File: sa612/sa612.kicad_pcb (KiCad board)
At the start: 2 copper layers, 12 parts, among them J1 RF_IN, J2 PWR, J3 OSC_IN, J4 IF_OUT, U1 SA612, U2 MCP1700-5002E_SOT23

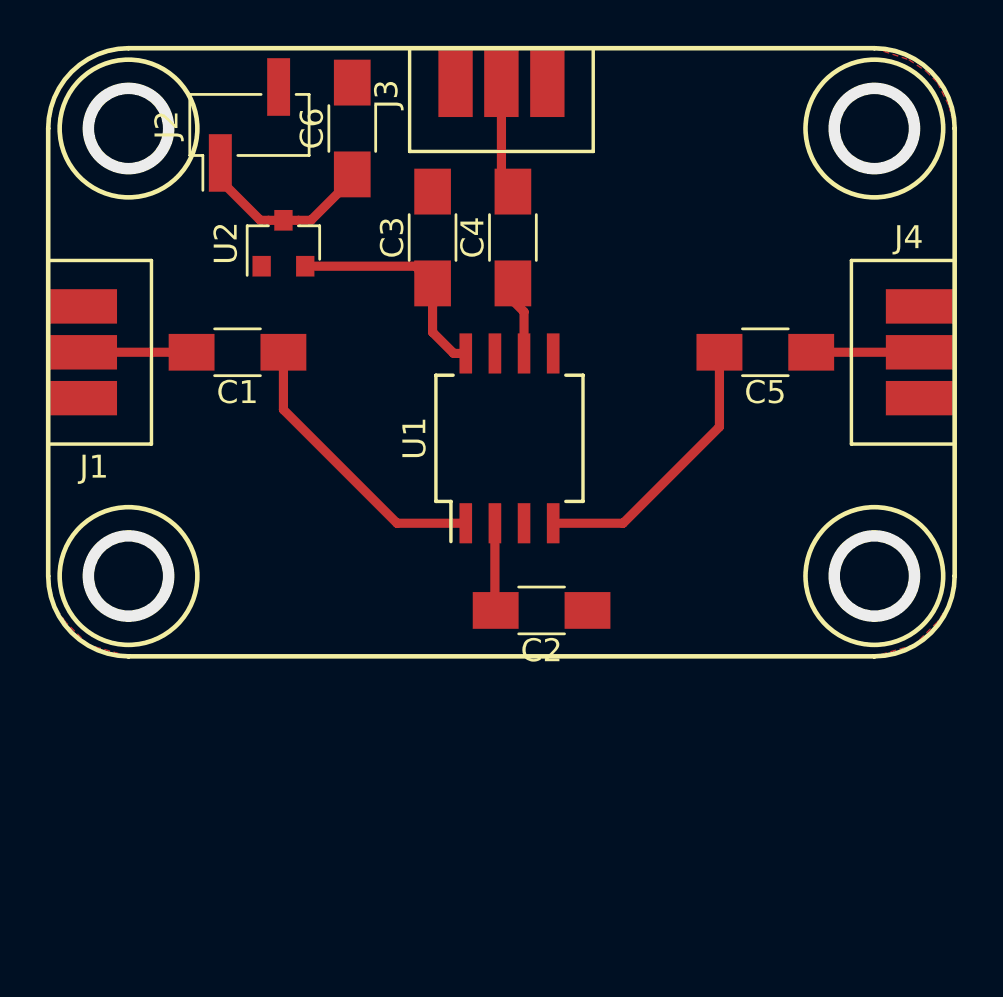
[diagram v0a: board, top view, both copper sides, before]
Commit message: Fix the sa612 board layout
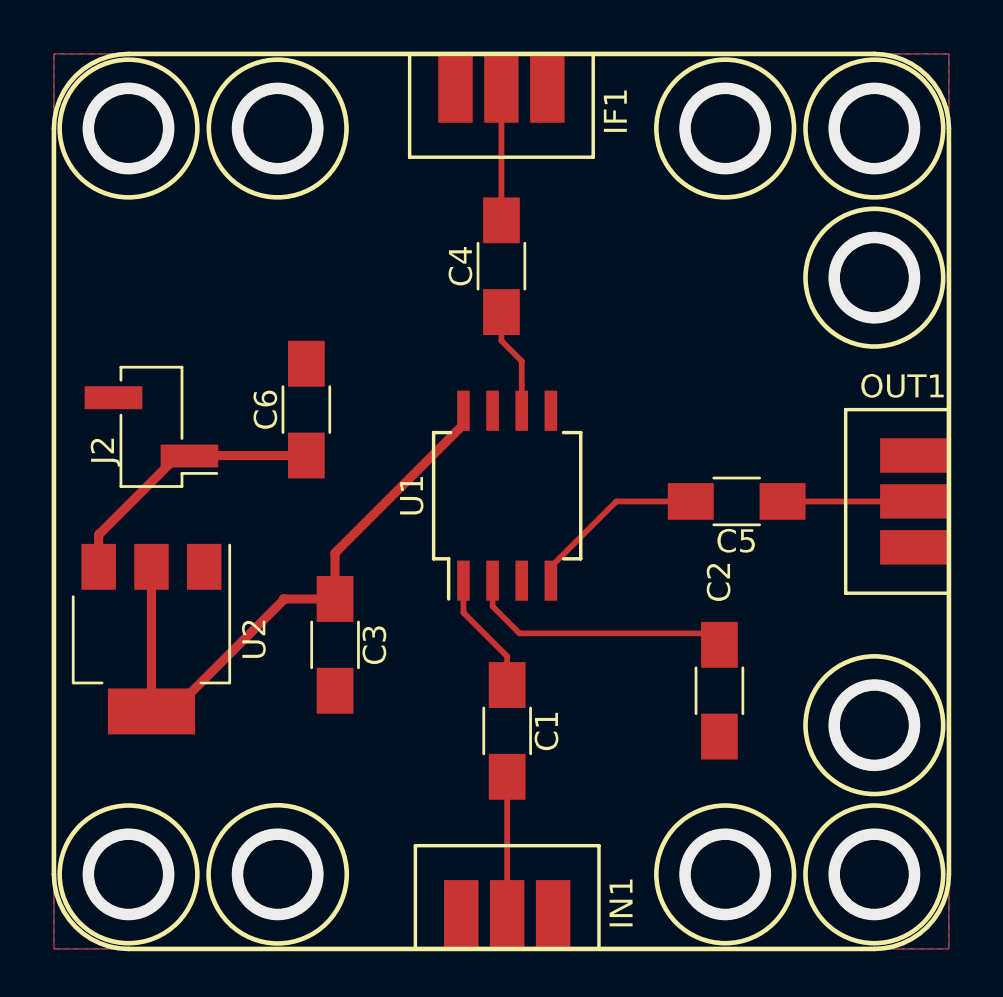
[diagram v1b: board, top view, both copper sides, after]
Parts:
- removed J4: IF_OUT, x-uhf:X-UHF_Interconnect
- added OUT1: RF_OUT, x-uhf:X-UHF_Interconnect, F.Cu at (144.2, 96.2)
- U2: value MCP1700-5002E_SOT23 -> LD1117S50TR_SOT223; footprint TO_SOT_Packages_SMD:SOT-23 -> TO_SOT_Packages_SMD:SOT-223-3_TabPin2
- moved IN1 30.7 mm to (126.5, 114.2), turned to 90 degrees
- moved C1 20.3 mm to (126.5, 106.2), turned to 270 degrees
- moved C3 18.3 mm to (119.0, 102.5), turned to 270 degrees
- moved U2 18.2 mm to (111.0, 102.2), turned to 270 degrees
- moved J2 13.8 mm to (111.0, 93.0), turned to 180 degrees
- moved C6 12.4 mm to (117.8, 92.2)
- moved C2 8.50 mm to (135.8, 104.5), turned to 90 degrees
- moved C5 6.62 mm to (136.5, 96.2)
- moved U1 2.50 mm to (126.5, 96.0)
- moved C4 1.35 mm to (126.2, 86.0)
- moved IF1 0.25 mm to (126.2, 78.2)
- renumbered J3 to IF1, J1 to IN1
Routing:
- net Net-(C3-Pad1): track 9.82 -> 27.0 mm
- net Net-(C2-Pad2): track 3.81 -> 11.8 mm
- net Net-(C1-Pad1): track 13.1 -> 5.34 mm
- net Net-(C5-Pad2): track 12.2 -> 7.88 mm
- net Net-(C6-Pad1): track 8.17 -> 11.9 mm
- net Net-(C4-Pad1): track 3.25 -> 4.67 mm
- net Net-(C1-Pad2): track 4.75 -> 6.05 mm
- net Net-(C5-Pad1): track 4.75 -> 5.75 mm
- net Net-(C4-Pad2): track 4.96 -> 5.75 mm
- net Earth: vias 0 -> 10
- net (no net): vias 4 -> 0
- added copper zone on B.Cu, net Earth
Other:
- rule trace_min: 0.4 -> 0.1
